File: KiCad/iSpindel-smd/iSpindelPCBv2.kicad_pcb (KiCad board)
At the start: 2 copper layers, 46 x 25 mm, 20 parts, among them J1 PROG, J2 PROG_con, SW1 SW_DPDT_x2, U1 MIC5219-3.3, U2 GY-521, U3 TP4056-shield-6PIN, U4 DS18B20, U5 LoRa_Ra-02, U6 ESP-07S

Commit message: adjust switch and charger
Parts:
- U3: footprint TP4056-shield-6PIN -> KiCadCustomLibs:TP4056-shield-6PIN
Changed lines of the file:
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@@
-(kicad_pcb (version 4) (host pcbnew 4.0.6)
+(kicad_pcb (version 4) (host pcbnew 4.0.7)
   (general
     (links 51)
     (no_connects 51)
-    (area 124.275 60.05 176.025001 92.938095)
+    (area 125.924999 65.924999 172.075001 91.075001)
     (thickness 1.6)
     (drawings 8)
@@
     (add_net VCC)
   )
-  (module TP4056-shield-6PIN (layer B.Cu)
-    (at 158.5 78.5 180)
-    (fp_text reference U3 (at 0.5 0 180) (layer B.SilkS)
-      (effects (font (size 1 1) (thickness 0.15)) (justify mirror))
-    )
-    (fp_text value TP4056-shield-6PIN (at 0 7 180) (layer B.Fab) hide
-      (effects (font (size 1 1) (thickness 0.15)) (justify mirror))
-    )
-    (fp_line (start -14.5 -4) (end -9.5 -4) (layer B.Fab) (width 0.15))
-    (fp_line (start 13 6) (end 13 -6) (layer B.SilkS) (width 0.15))
-    (fp_line (start 13 6) (end 14.5 6) (layer B.SilkS) (width 0.15))
-    (fp_line (start 14.5 6) (end 14.5 8.5) (layer B.SilkS) (width 0.15))
-    (fp_line (start 14.5 8.5) (end 13.5 8.5) (layer B.SilkS) (width 0.15))
-    (fp_line (start 13 -6) (end 14.5 -6) (layer B.SilkS) (width 0.15))
-    (fp_line (start 14.5 -6) (end 14.5 -8.5) (layer B.SilkS) (width 0.15))
-    (fp_line (start 14.5 -8.5) (end 13.5 -8.5) (layer B.SilkS) (width 0.15))
-    (fp_line (start -9.5 -4) (end -9.5 4) (layer B.Fab) (width 0.15))
-    (fp_line (start -9.5 4) (end -14.5 4) (layer B.Fab) (width 0.15))
-    (fp_line (start -14.5 4) (end -14.5 -4) (layer B.Fab) (width 0.15))
-    (fp_line (start -13.5 -8.5) (end -13.5 8.5) (layer B.SilkS) (width 0.15))
-    (fp_line (start -13.5 8.5) (end 13.5 8.5) (layer B.SilkS) (width 0.15))
-    (fp_line (start 13.5 -8.5) (end -13.5 -8.5) (layer B.SilkS) (width 0.15))
-    (pad 3 thru_hole oval (at 11.1 7 180) (size 3 2) (drill 1) (layers *.Cu *.Mask)
-      (net 20 "Net-(SW1-Pad2)"))
-    (pad 4 thru_hole oval (at 11.1 -7 180) (size 3 2) (drill 1) (layers *.Cu *.Mask)
-      (net 10 "Net-(U3-Pad4)"))
-    (pad 2 thru_hole oval (at -11.5 -7 180) (size 3 2) (drill 1) (layers *.Cu *.Mask)
-      (net 1 GND))
-    (pad 1 thru_hole oval (at -11.5 7 180) (size 3 2) (drill 1) (layers *.Cu *.Mask)
-      (net 11 "Net-(U3-Pad1)"))
-  )
   (module ESP-07S (layer F.Cu)
     (at 136.25 75.5 270)
@@
       (net 17 VCC))
   )
+  (module KiCadCustomLibs:TP4056-shield-6PIN (layer B.Cu)
+    (at 158.5 78.5 180)
+    (fp_text reference U3 (at 0.5 0 180) (layer B.SilkS)
+      (effects (font (size 1 1) (thickness 0.15)) (justify mirror))
+    )
+    (fp_text value TP4056-shield-6PIN (at 0 7 180) (layer B.Fab) hide
+      (effects (font (size 1 1) (thickness 0.15)) (justify mirror))
+    )
+    (fp_line (start -14.5 -4) (end -9.5 -4) (layer B.Fab) (width 0.15))
+    (fp_line (start 13 6) (end 13 -6) (layer B.SilkS) (width 0.15))
+    (fp_line (start 13 6) (end 14.5 6) (layer B.SilkS) (width 0.15))
+    (fp_line (start 14.5 6) (end 14.5 8.5) (layer B.SilkS) (width 0.15))
+    (fp_line (start 14.5 8.5) (end 13.5 8.5) (layer B.SilkS) (width 0.15))
+    (fp_line (start 13 -6) (end 14.5 -6) (layer B.SilkS) (width 0.15))
+    (fp_line (start 14.5 -6) (end 14.5 -8.5) (layer B.SilkS) (width 0.15))
+    (fp_line (start 14.5 -8.5) (end 13.5 -8.5) (layer B.SilkS) (width 0.15))
+    (fp_line (start -9.5 -4) (end -9.5 4) (layer B.Fab) (width 0.15))
+    (fp_line (start -9.5 4) (end -14.5 4) (layer B.Fab) (width 0.15))
+    (fp_line (start -14.5 4) (end -14.5 -4) (layer B.Fab) (width 0.15))
+    (fp_line (start -13.5 -8.5) (end -13.5 8.5) (layer B.SilkS) (width 0.15))
+    (fp_line (start -13.5 8.5) (end 13.5 8.5) (layer B.SilkS) (width 0.15))
+    (fp_line (start 13.5 -8.5) (end -13.5 -8.5) (layer B.SilkS) (width 0.15))
+    (pad 3 thru_hole oval (at 11.1 7 180) (size 3 2) (drill 1) (layers *.Cu *.Mask)
+      (net 20 "Net-(SW1-Pad2)"))
+    (pad 4 thru_hole oval (at 11.1 -7 180) (size 3 2) (drill 1) (layers *.Cu *.Mask)
+      (net 10 "Net-(U3-Pad4)"))
+    (pad 2 thru_hole oval (at -11.5 -7 180) (size 3 2) (drill 1) (layers *.Cu *.Mask)
+      (net 1 GND))
+    (pad 1 thru_hole oval (at -11.5 7 180) (size 3 2) (drill 1) (layers *.Cu *.Mask)
+      (net 11 "Net-(U3-Pad1)"))
+    (model ../../../../../../src/Tennp/Git/KiCadCustomLibs/wrl/TP4056shield.wrl
+      (at (xyz 0 0 0))
+      (scale (xyz 0.395 0.395 0.395))
+      (rotate (xyz 0 0 180))
+    )
+    (model ../../../../../../src/Tennp/Git/KiCadCustomLibs/wrl/Conn_USB-micro-2.0_socket_right-angle.wrl
+      (at (xyz -0.47 0 0.047))
+      (scale (xyz 1 1 1))
+      (rotate (xyz 0 0 0))
+    )
+  )
   (dimension 22.5 (width 0.3) (layer Dwgs.User)

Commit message: Some work still in progress
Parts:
- added D1: Schottky, Diodes_SMD:D_SOD-523, F.Cu at (146.0, 68.0)
- added REF**: MountingHole_3.2mm_M3, Mounting_Holes:MountingHole_3.2mm_M3, F.Cu at (163.3, 77.0)
- added REF**: MountingHole_3.2mm_M3, Mounting_Holes:MountingHole_3.2mm_M3, F.Cu at (148.3, 77.0)
- added REF**: MountingHole_3.2mm_M3, Mounting_Holes:MountingHole_3.2mm_M3, F.Cu at (170.0, 89.0)
- added REF**: MountingHole_3.2mm_M3, Mounting_Holes:MountingHole_3.2mm_M3, F.Cu at (170.0, 68.0)
- SW1: value SW_DPDT_x2 -> SW_SPDT
- moved J2 7.50 mm to (134.5, 88.9), turned to 90 degrees
- moved R2 5.17 mm to (126.6, 80.8), turned to 270 degrees
- moved R4 4.26 mm to (150.0, 68.0)
- moved C3 3.76 mm to (160.5, 67.5)
- moved C2 3.75 mm to (163.5, 70.5)
- moved U1 3.75 mm to (160.5, 70.5)
- moved C5 3.60 mm to (126.6, 70.9)
- moved C1 3.50 mm to (157.0, 70.5), turned to 270 degrees
- moved C4 3.35 mm to (126.6, 74.4)
- moved R1 3.01 mm to (154.0, 68.0)
- moved R3 2.76 mm to (152.0, 68.0), turned to 270 degrees
- moved R6 1.61 mm to (130.2, 85.8), turned to 0 degrees
- moved R5 0.56 mm to (148.0, 68.0)
- moved U5 0.42 mm to (134.6, 75.0)
- moved U3 0.17 mm to (158.3, 78.5)
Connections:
- J2 pad 4: VCC -> /VCC_PROG
- SW1 pad 1: VCC -> /VCC_PROG
- SW1 pad 2: Net-(SW1-Pad2) -> VCC
- U2 pad 5: Net-(U2-Pad5) -> (no net)
- U2 pad 6: Net-(U2-Pad6) -> (no net)
- U2 pad 7: Net-(U2-Pad7) -> (no net)
- U2 pad 8: Net-(U2-Pad8) -> (no net)
- U3 pad 1: Net-(U3-Pad1) -> (no net)
- U3 pad 3: Net-(SW1-Pad2) -> Net-(SW1-Pad3)
- U3 pad 4: Net-(U3-Pad4) -> (no net)
- U5 pad 10: Net-(U5-Pad10) -> (no net)
- U5 pad 11: Net-(U5-Pad11) -> (no net)
- U5 pad 5: Net-(U5-Pad5) -> (no net)
- U5 pad 6: Net-(U5-Pad6) -> (no net)
- U5 pad 7: Net-(U5-Pad7) -> (no net)
- U5 pad 8: Net-(U5-Pad8) -> (no net)
- U6 pad 13: Net-(U6-Pad13) -> (no net)
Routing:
- net GND: track 0.00 -> 89.4 mm, vias 0 -> 28
- net VCC: track 0.00 -> 73.6 mm
- net +3V3: track 0.00 -> 67.5 mm, vias 0 -> 4
- net /SDA: track 0.00 -> 30.6 mm, vias 0 -> 4
- net /SCL: track 0.00 -> 28.0 mm, vias 0 -> 2
- net /RES: track 0.00 -> 25.9 mm, vias 0 -> 1
- net /Temp: track 0.00 -> 24.7 mm
- net Net-(SW1-Pad3): track 0.00 -> 24.5 mm, vias 0 -> 1
- net Net-(R1-Pad2): track 0.00 -> 23.1 mm, vias 0 -> 2
- net /NSS: track 0.00 -> 18.3 mm, vias 0 -> 1
- net /MOSI: track 0.00 -> 17.4 mm, vias 0 -> 1
- net /MISO: track 0.00 -> 14.4 mm, vias 0 -> 1
- net /EN: track 0.00 -> 14.0 mm, vias 0 -> 2
- net /SCK: track 0.00 -> 11.3 mm, vias 0 -> 1
- net Net-(J2-Pad2): track 0.00 -> 9.74 mm
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- added copper zone on B.Cu, net GND
- added copper zone on F.Cu, net GND
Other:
- board size 46 x 25 mm -> 46.5 x 25 mm
- net class Default: trace_width 0.25 -> 0.4; via_dia 0.6 -> 0.7
- net class VCC added: clearance 0.2, trace_width 0.7, via_dia 1, via_drill 0.6
- rule pad_to_mask_clearance: 0.2 -> 0.15
- board text added: "DS18B20"
- board text added: "GND"
- board text added: "LoRa Ra-02"
- board text added: "OUT+"
- board text added: "RX"
- board text added: "TP4056"
- board text added: "TX"
- board text added: "VCC"
- board text added: "short for prog"
- board text added: "www.ispindel.de"

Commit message: adjusted some tracks
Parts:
- U3: footprint KiCadCustomLibs:TP4056-shield-6PIN -> TP4056-shield-6PIN
- moved C1 2.00 mm to (157.0, 68.5), turned to 90 degrees
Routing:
- net /VCC_PROG: track 0.00 -> 31.6 mm, vias 0 -> 2
- net VCC: track 73.6 -> 79.9 mm
- net GND: track 89.4 -> 89.6 mm, vias 28 -> 30

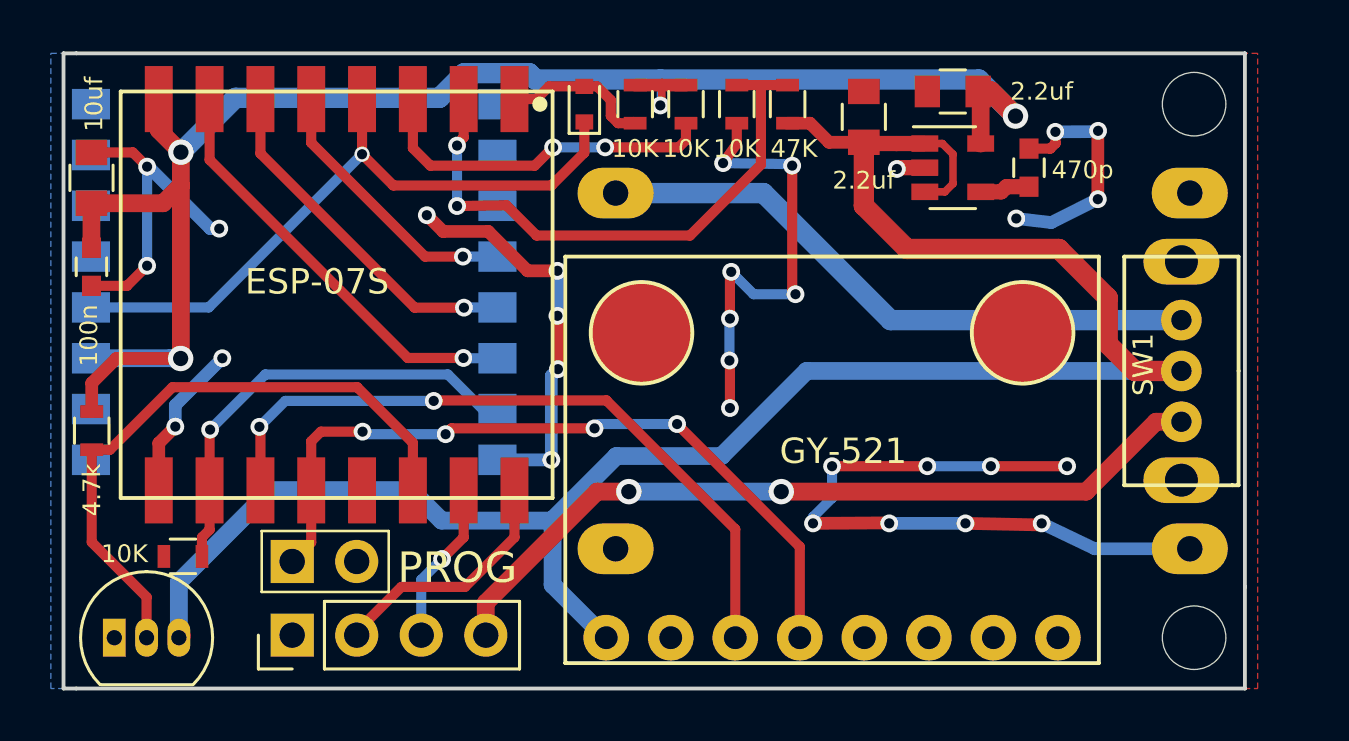
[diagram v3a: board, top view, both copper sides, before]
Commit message: Add TH variant
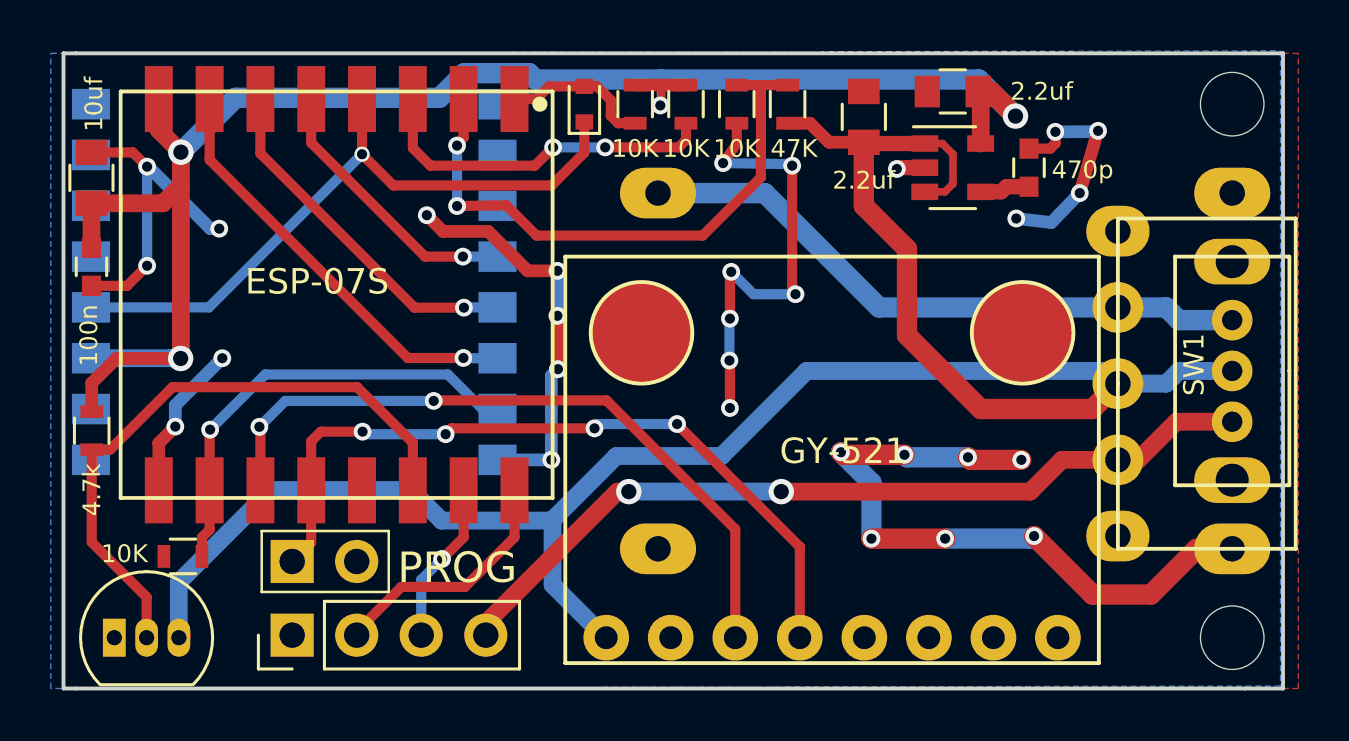
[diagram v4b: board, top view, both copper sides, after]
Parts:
- added SW2: SW_SPDT, KiCadCustomLibs:SS-12F23, F.Cu at (167.0, 79.0)
- moved SW1 2.00 mm to (171.5, 78.5)
- moved U3 1.67 mm to (160.0, 78.5)
- moved REF** 1.50 mm to (171.5, 89.0)
- moved REF** 1.50 mm to (171.5, 68.0)
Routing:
- net VCC: track 79.9 -> 81.8 mm
- net /VCC_PROG: track 31.6 -> 33.1 mm
- net GND: track 89.6 -> 89.2 mm, vias 30 -> 29
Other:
- board size 46.5 x 25 mm -> 48 x 25 mm

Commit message: Add led
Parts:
- added C6: 100n, Capacitors_SMD:C_0603, F.Cu at (165.5, 69.0)
- added D2: LED, LEDs:LED_0805, F.Cu at (169.0, 88.6)
- added R7: 4.7k, Resistors_SMD:R_0603, F.Cu at (167.2, 87.9)
- added SW3: SW_Push, KiCadCustomLibs:Button_TS-018, F.Cu at (168.5, 69.0)
- moved U1 0.71 mm to (161.0, 71.0)
- moved C3 0.50 mm to (160.5, 68.0)
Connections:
- U6 pad 13: (no net) -> /LED
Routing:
- net /LED: track 0.00 -> 64.1 mm, vias 0 -> 2
- net +3V3: track 67.5 -> 96.8 mm, vias 4 -> 5
- net Net-(C6-Pad1): track 5.99 -> 30.1 mm
- net GND: track 89.2 -> 92.9 mm, vias 29 -> 32
- net Net-(D2-Pad2): track 0.00 -> 2.57 mm
- net /Temp: track 24.7 -> 25.6 mm
- net /SCL: track 28.0 -> 28.8 mm
- net VCC: track 81.8 -> 82.4 mm
- net /NSS: track 18.3 -> 19.0 mm
